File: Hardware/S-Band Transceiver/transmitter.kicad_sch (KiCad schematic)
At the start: 42 parts, among them J5 SMA-J-P-H-ST-EM1, U10 TSS-53LNB3+, U11 DCW-22-332+, U12 ADL5906, U7 DAT-31A+, U8 PE44820, U9 SN74LVC1G125DCK

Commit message: Fixing issue with phase shifter schematic
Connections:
- net GND: now also U8.29 (D3/A3), U8.30 (D2/A2), U8.31 (D1/A1), U8.32 (D0/A0)
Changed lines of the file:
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@@
+	)
+	(junction
+		(at 135.89 86.36)
+		(diameter 0)
+		(color 0 0 0 0)
 	)
 	(junction
@@
 		(color 0 0 0 0)
 	)
+	(junction
+		(at 135.89 81.28)
+		(diameter 0)
+		(color 0 0 0 0)
+	)
+	(junction
+		(at 135.89 83.82)
+		(diameter 0)
+		(color 0 0 0 0)
+	)
 	(wire
 		(pts
@@
 	(wire
 		(pts
+			(xy 133.35 78.74) (xy 135.89 78.74)
+		)
+		(stroke
+			(width 0)
+			(type default)
+		)
+	)
+	(wire
+		(pts
 			(xy 72.39 88.9) (xy 67.31 88.9)
 		)
@@
 	(wire
 		(pts
+			(xy 133.35 81.28) (xy 135.89 81.28)
+		)
+		(stroke
+			(width 0)
+			(type default)
+		)
+	)
+	(wire
+		(pts
 			(xy 133.35 66.04) (xy 135.89 66.04)
 		)
@@
 	(wire
 		(pts
+			(xy 135.89 81.28) (xy 135.89 83.82)
+		)
+		(stroke
+			(width 0)
+			(type default)
+		)
+	)
+	(wire
+		(pts
 			(xy 44.45 66.04) (xy 41.91 66.04)
 		)
@@
 	(wire
 		(pts
+			(xy 133.35 86.36) (xy 135.89 86.36)
+		)
+		(stroke
+			(width 0)
+			(type default)
+		)
+	)
+	(wire
+		(pts
+			(xy 135.89 78.74) (xy 135.89 81.28)
+		)
+		(stroke
+			(width 0)
+			(type default)
+		)
+	)
+	(wire
+		(pts
 			(xy 191.77 31.75) (xy 195.58 31.75)
 		)
@@
 	(wire
 		(pts
+			(xy 135.89 83.82) (xy 135.89 86.36)
+		)
+		(stroke
+			(width 0)
+			(type default)
+		)
+	)
+	(wire
+		(pts
 			(xy 102.87 43.18) (xy 104.14 43.18)
 		)
@@
 	(wire
 		(pts
+			(xy 133.35 83.82) (xy 135.89 83.82)
+		)
+		(stroke
+			(width 0)
+			(type default)
+		)
+	)
+	(wire
+		(pts
 			(xy 110.49 92.71) (xy 110.49 93.98)
 		)
@@
 		(pts
 			(xy 236.22 101.6) (xy 236.22 102.87)
+		)
+		(stroke
+			(width 0)
+			(type default)
+		)
+	)
+	(wire
+		(pts
+			(xy 135.89 86.36) (xy 135.89 87.63)
 		)
 		(stroke
@@
 					(unit 1)
 				)
+			)
+		)
+	)
+	(symbol
+		(lib_id "power:GND")
+		(at 135.89 87.63 0)
+		(unit 1)
+		(exclude_from_sim no)
+		(in_bom yes)
+		(on_board yes)
+		(dnp no)
+		(fields_autoplaced yes)
+		(property "Reference" "#PWR0145"
+			(at 135.89 93.98 0)
+			(effects
+				(font
+					(size 1.27 1.27)
+				)
+				(hide yes)
+			)
+		)
+		(property "Value" "GND"
+			(at 135.89 92.71 0)
+			(effects
+				(font
+					(size 1.27 1.27)
+				)
+			)
+		)
+		(property "Footprint" ""
+			(at 135.89 87.63 0)
+			(effects
+				(font
+					(size 1.27 1.27)
+				)
+				(hide yes)
+			)
+		)
+		(property "Datasheet" ""
+			(at 135.89 87.63 0)
+			(effects
+				(font
+					(size 1.27 1.27)
+				)
+				(hide yes)
+			)
+		)
+		(property "Description" "Power symbol creates a global label with name \"GND\" , ground"
+			(at 135.89 87.63 0)
+			(effects
+				(font
+					(size 1.27 1.27)
+				)
+				(hide yes)
+			)
+		)
+		(pin "1"
+		)
+		(instances
+			(project "S-Band Transceiver"
+				(path "/811f57cf-e3df-4fba-aff9-353adc85299e/bd41cfbd-cb46-4539-92e1-7ba2287bca8a"
+					(reference "#PWR0145")
+					(unit 1)
+				)

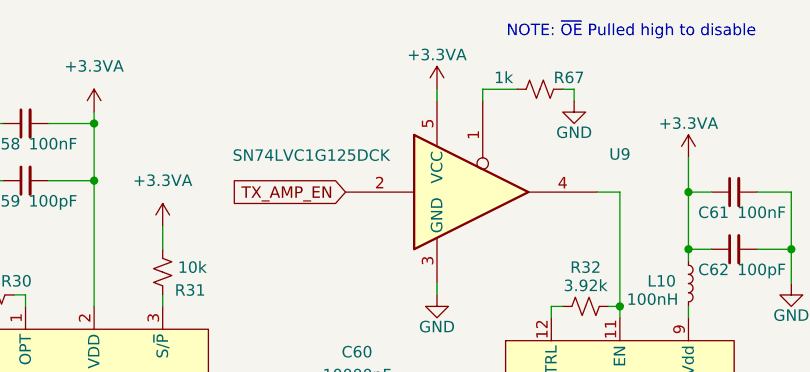
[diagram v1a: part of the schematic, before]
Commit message: Adding decoupling capacitor
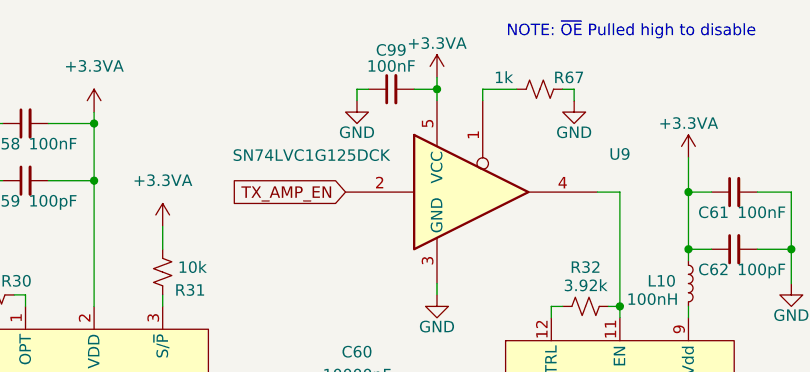
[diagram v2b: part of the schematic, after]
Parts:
- added C99: 100nF, Capacitor_SMD:C_0402_1005Metric, symbol Device:C_Small
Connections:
- net +3.3VA: now also C99.2
- net GND: now also C99.1
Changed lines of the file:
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@@
 	)
 	(junction
+		(at 156.21 20.32)
+		(diameter 0)
+		(color 0 0 0 0)
+	)
+	(junction
 		(at 67.31 88.9)
 		(diameter 0)
@@
 	(wire
 		(pts
+			(xy 156.21 20.32) (xy 156.21 21.59)
+		)
+		(stroke
+			(width 0)
+			(type default)
+		)
+	)
+	(wire
+		(pts
 			(xy 71.12 34.29) (xy 71.12 31.75)
 		)
@@
 	(wire
 		(pts
+			(xy 153.67 20.32) (xy 156.21 20.32)
+		)
+		(stroke
+			(width 0)
+			(type default)
+		)
+	)
+	(wire
+		(pts
 			(xy 110.49 43.18) (xy 110.49 44.45)
 		)
@@
 	(wire
 		(pts
+			(xy 147.32 20.32) (xy 148.59 20.32)
+		)
+		(stroke
+			(width 0)
+			(type default)
+		)
+	)
+	(wire
+		(pts
 			(xy 82.55 73.66) (xy 83.82 73.66)
 		)
@@
 	(wire
 		(pts
+			(xy 147.32 21.59) (xy 147.32 20.32)
+		)
+		(stroke
+			(width 0)
+			(type default)
+		)
+	)
+	(wire
+		(pts
 			(xy 223.52 101.6) (xy 223.52 105.41)
 		)
@@
 	(wire
 		(pts
-			(xy 156.21 20.32) (xy 156.21 21.59)
+			(xy 156.21 19.05) (xy 156.21 20.32)
 		)
 		(stroke
@@
 	(symbol
 		(lib_id "Device:C_Small")
+		(at 151.13 20.32 90)
+		(unit 1)
+		(exclude_from_sim no)
+		(in_bom yes)
+		(on_board yes)
+		(dnp no)
+		(property "Reference" "C99"
+			(at 151.13 16.002 90)
+			(effects
+				(font
+					(size 1.27 1.27)
+				)
+			)
+		)
+		(property "Value" "100nF"
+			(at 151.13 17.78 90)
+			(effects
+				(font
+					(size 1.27 1.27)
+				)
+			)
+		)
+		(property "Footprint" "Capacitor_SMD:C_0402_1005Metric"
+			(at 151.13 20.32 0)
+			(effects
+				(font
+					(size 1.27 1.27)
+				)
+				(hide yes)
+			)
+		)
+		(property "Datasheet" "~"
+			(at 151.13 20.32 0)
+			(effects
+				(font
+					(size 1.27 1.27)
+				)
+				(hide yes)
+			)
+		)
+		(property "Description" "Unpolarized capacitor, small symbol"
+			(at 151.13 20.32 0)
+			(effects
+				(font
+					(size 1.27 1.27)
+				)
+				(hide yes)
+			)
+		)
+		(pin "2"
+		)
+		(pin "1"
+		)
+		(instances
+			(project "S-Band Transceiver"
+				(path "/811f57cf-e3df-4fba-aff9-353adc85299e/bd41cfbd-cb46-4539-92e1-7ba2287bca8a"
+					(reference "C99")
+					(unit 1)
+				)
+			)
+		)
+	)
+	(symbol
+		(lib_id "Device:C_Small")
 		(at 76.2 40.64 90)
 		(unit 1)
@@
 	(symbol
 		(lib_id "power:GND")
+		(at 147.32 21.59 0)
+		(unit 1)
+		(exclude_from_sim no)
+		(in_bom yes)
+		(on_board yes)
+		(dnp no)
+		(property "Reference" "#PWR0147"
+			(at 147.32 27.94 0)
+			(effects
+				(font
+					(size 1.27 1.27)
+				)
+				(hide yes)
+			)
+		)
+		(property "Value" "GND"
+			(at 147.32 25.146 0)
+			(effects
+				(font
+					(size 1.27 1.27)
+				)
+			)
+		)
+		(property "Footprint" ""
+			(at 147.32 21.59 0)
+			(effects
+				(font
+					(size 1.27 1.27)
+				)
+				(hide yes)
+			)
+		)
+		(property "Datasheet" ""
+			(at 147.32 21.59 0)
+			(effects
+				(font
+					(size 1.27 1.27)
+				)
+				(hide yes)
+			)
+		)
+		(property "Description" "Power symbol creates a global label with name \"GND\" , ground"
+			(at 147.32 21.59 0)
+			(effects
+				(font
+					(size 1.27 1.27)
+				)
+				(hide yes)
+			)
+		)
+		(pin "1"
+		)
+		(instances
+			(project "S-Band Transceiver"
+				(path "/811f57cf-e3df-4fba-aff9-353adc85299e/bd41cfbd-cb46-4539-92e1-7ba2287bca8a"
+					(reference "#PWR0147")
+					(unit 1)
+				)
+			)
+		)
+	)
+	(symbol
+		(lib_id "power:GND")
 		(at 83.82 83.82 0)
 		(unit 1)
@@
 	(symbol
 		(lib_id "power:+3.3VA")
-		(at 156.21 20.32 0)
+		(at 156.21 19.05 0)
 		(unit 1)
 		(exclude_from_sim no)
@@
 		(dnp no)
 		(property "Reference" "#PWR083"
-			(at 156.21 24.13 0)
+			(at 156.21 22.86 0)
 			(effects
 				(font
@@
 		)
 		(property "Value" "+3.3VA"
-			(at 156.21 16.51 0)
+			(at 156.21 15.24 0)
 			(effects
 				(font
@@
 		)
 		(property "Footprint" ""
-			(at 156.21 20.32 0)
+			(at 156.21 19.05 0)
 			(effects
 				(font
@@
 		)
 		(property "Datasheet" ""
-			(at 156.21 20.32 0)
+			(at 156.21 19.05 0)
 			(effects
 				(font
@@
 		)
 		(property "Description" "Power symbol creates a global label with name \"+3.3VA\""
-			(at 156.21 20.32 0)
+			(at 156.21 19.05 0)
 			(effects
 				(font
